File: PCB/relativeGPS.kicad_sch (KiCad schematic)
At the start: 0 parts

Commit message: Progress
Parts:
- added C1, C2: C_120pF_50V_5%_C0G_0402_H0.55, 002-Capacitors:C_0402_H0.55, symbol 002-Capacitors:C_120pF_50V_5%_C0G_0402
- added C3: C_22uF_6.3V_20%_X5R_0805_H1.4, 002-Capacitors:C_0805_H1.4, symbol 002-Capacitors:C_22uF_6.3V_20%_X5R_0805
- added C4: C_4.7uF_10V_10%_X7S_0603_H0.95, 002-Capacitors:C_0603_H0.95, symbol 002-Capacitors:C_4.7uF_10V_10%_X7S_0603
- added C5: C_10nF_50V_10%_X7R_0402_H0.55, 002-Capacitors:C_0402_H0.55, symbol 002-Capacitors:C_10nF_50V_10%_X7R_0402
- added C6: C_56pF_50V_2%_C0G_0201_H0.33, 002-Capacitors:C_0402_H0.55, symbol 002-Capacitors:C_56pF_50V_2%_C0G_0201
- added CN1: PPPC051LGBN-RC, 009-Connectors:PPPC051LGBN-RC, symbol 009-Connectors:PPPC051LGBN-RC
- added L1: L_5.6nH_2%_1.77A_40mOhm, 003-Inductors:LQW15AN5N6G80D, symbol 003-Inductors:L_5.6nH_2%_1.77A_40mOhm
- added L2: L_10uH_20%_1.51A_160mOhm, 003-Inductors:LTF5022T-100M1R3-D, symbol 003-Inductors:L_10uH_20%_1.51A_160mOhm
- added L3: L_27nH_5%_0.35A_460mOhm, 003-Inductors:LQG15HS27NJ02D, symbol 003-Inductors:L_27nH_5%_0.35A_460mOhm
- added R1: R_10k_5%_1/16W_0402, 001-Resistors:R_0402_H0.4, symbol 001-Resistors:R_10k_5%_1/16W_0402
- added R2: R_15k_1%_1/16W_0402, 001-Resistors:R_0402_H0.4, symbol 001-Resistors:R_15k_1%_1/16W_0402
- added R3: R_68k_1%_1/16W_0402, 001-Resistors:R_0402_H0.4, symbol 001-Resistors:R_68k_1%_1/16W_0402
- added R4: R_1M_5%_1/16W_0402, 001-Resistors:R_0402_H0.4, symbol 001-Resistors:R_1M_5%_1/16W_0402
- added U1: TCA39306DCUR, 005-ICs:TCA39306DCUR, symbol 005-ICs:TCA39306DCUR
- added U2: LSM303AH, 008-Sensors:LSM303AHTR, symbol 008-Sensors:LSM303AHTR
- added U3: TESEO-LIV3R, 010-RF:TESEO-LIV3R, symbol 010-RF:TESEO-LIV3R
- added U4: BGA725L6E6327FTSA1, 010-RF:BGA725L6E6327FTSA1, symbol 010-RF:BGA725L6E6327FTSA1
- added U5: B39162B4327P810, 010-RF:B39162B4327P810, symbol 010-RF:B39162B4327P810
- added U6: ST1S12GR, 004-Power:ST1S12GR, symbol 004-Power:ST1S12GR
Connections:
- new net: C2.2, U3.11 (RF_IN)
- new net: L2.1, R3.1, U6.3 (SW)
- new net: R2.1, R3.2, U6.5 (FB)
- new net: U4.3 (OUT), U5.1 (IN)
- new net: L1.2, U4.5 (IN)
- new net: R4.2, U6.1 (EN)
- new net: C4.2, R4.1, U6.4 (IN)
- new net: C2.1, U5.4 (OUT)
- new net: C1.2, L1.1
- new net +1V8: U1.2 (VREF1), U2.10 (VDD_IO), U2.2 (CS), U2.9 (VDD)
- new net +3.3V: CN1.1
- new net 3V3_TESEO: C3.1, C5.1, L2.2, L3.1
- new net 3V3_TESEO_FILTERED: C6.1, L3.2, U3.6 (Vbat), U3.7 (VCC_IO), U3.8 (VCC)
- new net ANTOFF: R1.1, U3.13 (AntOFF), U4.6 (PON)
- new net GND: C3.2, C4.1, C5.2, C6.2, CN1.5, R1.2, R2.2, U1.1 (GND), U2.6 (GND), U2.8 (GND), U4.1 (GND), U4.4 (GNDRF), U5.2 (GND), U5.3 (GND), U5.5 (GND), U6.2 (GND)
- new net RYLR998_RST: CN1.2
- new net RYLR998_RX: CN1.3
- new net RYLR998_TX: CN1.4
- new net SCL_1V8: U1.3 (SCL1), U2.1 (SCL/SPC)
- new net SDA_1V8: U1.4 (SDA1), U2.4 (SDA/SDI/SDO)
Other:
- note added: "100nF + 10uF on vdd 100nF to vdd_io"
- note added: "220nF"
- note added: "5V ?"
- note added: "GPS"
- note added: "LoRa module"
- note added: "Magnetometer + accelerometer"

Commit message: Remove useless backup files
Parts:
- added ANT1: ANT2525B00DT1516S, 010-RF:ANT2525B00DT1516S, symbol 010-RF:ANT2525B00DT1516S
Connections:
- net at C1.1: now also ANT1.1
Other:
- note added: "Add R0"
- note added: "Add jumper"
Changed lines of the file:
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@@
 	(wire
 		(pts
+			(xy 148.59 81.28) (xy 154.94 81.28)
+		)
+		(stroke
+			(width 0)
+			(type default)
+		)
+	)
+	(wire
+		(pts
 			(xy 81.28 80.01) (xy 68.58 80.01)
 		)
@@
 	(wire
 		(pts
+			(xy 148.59 78.74) (xy 148.59 81.28)
+		)
+		(stroke
+			(width 0)
+			(type default)
+		)
+	)
+	(wire
+		(pts
 			(xy 251.46 48.26) (xy 266.7 48.26)
 		)
@@
 	(wire
 		(pts
-			(xy 149.86 81.28) (xy 154.94 81.28)
-		)
-		(stroke
-			(width 0)
-			(type default)
-		)
-	)
-	(wire
-		(pts
 			(xy 254 62.23) (xy 254 68.58)
 		)
@@
 		)
 	)
+	(text "Add jumper"
+		(exclude_from_sim no)
+		(at 189.484 67.056 0)
+		(effects
+			(font
+				(size 1.27 1.27)
+			)
+		)
+	)
 	(text "220nF"
 		(exclude_from_sim no)
@@
 		)
 	)
+	(text "Add R0\n"
+		(exclude_from_sim no)
+		(at 201.93 70.104 0)
+		(effects
+			(font
+				(size 1.27 1.27)
+			)
+		)
+	)
 	(text "100nF + 10uF on vdd\n100nF to vdd_io\n"
 		(exclude_from_sim no)
@@
 					(unit 1)
 				)
+			)
+		)
+	)
+	(symbol
+		(lib_id "010-RF:ANT2525B00DT1516S")
+		(at 148.59 76.2 0)
+		(unit 1)
+		(exclude_from_sim no)
+		(in_bom yes)
+		(on_board yes)
+		(dnp no)
+		(property "Reference" "ANT1"
+			(at 139.7 74.168 0)
+			(effects
+				(font
+					(size 1.27 1.27)
+				)
+				(justify left)
+			)
+		)
+		(property "Value" "ANT2525B00DT1516S"
+			(at 148.59 86.868 0)
+			(effects
+				(font
+					(size 1.27 1.27)
+				)
+				(hide yes)
+			)
+		)
+		(property "Footprint" "010-RF:ANT2525B00DT1516S"
+			(at 148.59 99.314 0)
+			(effects
+				(font
+					(size 1.27 1.27)
+				)
+				(hide yes)
+			)
+		)
+		(property "Datasheet" "https://productfinder.pulseelectronics.com/api/open/part-attachments/datasheet/ANT2525B00DT1516S"
+			(at 148.59 93.726 0)
+			(effects
+				(font
+					(size 1.27 1.27)
+				)
+				(hide yes)
+			)
+		)
+		(property "Description" "GNSS Antenna, patch, through-hole"
+			(at 148.59 101.346 0)
+			(effects
+				(font
+					(size 1.27 1.27)
+				)
+				(hide yes)
+			)
+		)
+		(property "Web link" "https://www.digikey.ch/en/products/detail/pulse-electronics/ANT2525B00DT1516S/3927219?s=N4IgTCBcDaIIIDkAqYCsaBCAGLARJAjKgQGwDKIAugL5A"
+			(at 148.59 91.44 0)
+			(effects
+				(font
+					(size 1.27 1.27)
+				)
+				(hide yes)
+			)
+		)
+		(property "Manufacturer" "Pulse Electronics"
+			(at 148.59 88.9 0)
+			(effects
+				(font
+					(size 1.27 1.27)
+				)
+				(hide yes)
+			)
+		)
+		(property "Manufacturer P/N" "ANT2525B00DT1516S"
+			(at 148.844 103.632 0)
+			(effects
+				(font
+					(size 1.27 1.27)
+				)
+				(hide yes)
+			)
+		)
+		(property "Digikey P/N" "311-1539-ND"
+			(at 148.844 96.266 0)
+			(effects
+				(font
+					(size 1.27 1.27)
+				)
+				(hide yes)
+			)
+		)
+		(property "Price" "2.48"
+			(at 148.59 108.204 0)
+			(effects
+				(font
+					(size 1.27 1.27)
+				)
+				(hide yes)
+			)
+		)
+		(property "Height" "4"
+			(at 148.59 109.982 0)
+			(effects
+				(font
+					(size 1.27 1.27)
+				)
+				(hide yes)
+			)
+		)
+		(property "Temperature" "-40 to 105"
+			(at 148.59 105.918 0)
+			(effects
+				(font
+					(size 1.27 1.27)
+				)
+				(hide yes)
+			)
+		)
+		(property "Value Disp" "ANT 25x25"
+			(at 136.144 76.454 0)
+			(effects
+				(font
+					(size 1.27 1.27)
+				)
+				(justify left)
+			)
+		)
+		(pin "1"
+		)
+		(instances
+			(project "relativeGPS"
+				(path "/9255e348-2f0c-48d3-8a71-46491dcb1a12"
+					(reference "ANT1")
+					(unit 1)
+				)

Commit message: WIP
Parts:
- removed ANT1: ANT2525B00DT1516S, 010-RF:ANT2525B00DT1516S, symbol 010-RF:ANT2525B00DT1516S
- removed C1, C2: C_120pF_50V_5%_C0G_0402_H0.55, 002-Capacitors:C_0402_H0.55, symbol 002-Capacitors:C_120pF_50V_5%_C0G_0402
- removed C3: C_22uF_6.3V_20%_X5R_0805_H1.4, 002-Capacitors:C_0805_H1.4, symbol 002-Capacitors:C_22uF_6.3V_20%_X5R_0805
- removed C4: C_4.7uF_10V_10%_X7S_0603_H0.95, 002-Capacitors:C_0603_H0.95, symbol 002-Capacitors:C_4.7uF_10V_10%_X7S_0603
- removed C5: C_10nF_50V_10%_X7R_0402_H0.55, 002-Capacitors:C_0402_H0.55, symbol 002-Capacitors:C_10nF_50V_10%_X7R_0402
- removed C6: C_56pF_50V_2%_C0G_0201_H0.33, 002-Capacitors:C_0402_H0.55, symbol 002-Capacitors:C_56pF_50V_2%_C0G_0201
- removed L1: L_5.6nH_2%_1.77A_40mOhm, 003-Inductors:LQW15AN5N6G80D, symbol 003-Inductors:L_5.6nH_2%_1.77A_40mOhm
- removed L2: L_10uH_20%_1.51A_160mOhm, 003-Inductors:LTF5022T-100M1R3-D, symbol 003-Inductors:L_10uH_20%_1.51A_160mOhm
- removed L3: L_27nH_5%_0.35A_460mOhm, 003-Inductors:LQG15HS27NJ02D, symbol 003-Inductors:L_27nH_5%_0.35A_460mOhm
- removed R1: R_10k_5%_1/16W_0402, 001-Resistors:R_0402_H0.4, symbol 001-Resistors:R_10k_5%_1/16W_0402
- removed R2: R_15k_1%_1/16W_0402, 001-Resistors:R_0402_H0.4, symbol 001-Resistors:R_15k_1%_1/16W_0402
- removed R3: R_68k_1%_1/16W_0402, 001-Resistors:R_0402_H0.4, symbol 001-Resistors:R_68k_1%_1/16W_0402
- removed R4: R_1M_5%_1/16W_0402, 001-Resistors:R_0402_H0.4, symbol 001-Resistors:R_1M_5%_1/16W_0402
- removed U1: TCA39306DCUR, 005-ICs:TCA39306DCUR, symbol 005-ICs:TCA39306DCUR
- removed U2: LSM303AH, 008-Sensors:LSM303AHTR, symbol 008-Sensors:LSM303AHTR
- removed U3: TESEO-LIV3R, 010-RF:TESEO-LIV3R, symbol 010-RF:TESEO-LIV3R
- removed U4: BGA725L6E6327FTSA1, 010-RF:BGA725L6E6327FTSA1, symbol 010-RF:BGA725L6E6327FTSA1
- removed U5: B39162B4327P810, 010-RF:B39162B4327P810, symbol 010-RF:B39162B4327P810
- removed U6: ST1S12GR, 004-Power:ST1S12GR, symbol 004-Power:ST1S12GR
- added C10, C11, C9: C_1uF_50V_10%_X5R_0603_H0.9, 002-Capacitors:C_0603_H0.95, symbol 002-Capacitors:C_1uF_50V_10%_X5R_0603
- added C8: C_100nF_50V_10%_X7R_0402_H0.55, 002-Capacitors:C_0402_H0.55, symbol 002-Capacitors:C_100nF_50V_10%_X7R_0402
- added IC1: MIC5330-SSYML-TR, 004-Power:MIC5330, symbol 004-Power:MIC5330-SSYML-TR
- added R10, R9: R_4k7_1%_1/10W_0603, 001-Resistors:R_0603_H0.55, symbol 001-Resistors:R_4k7_1%_1/10W_0603
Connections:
- net +3.3V: now also C10.1, IC1.8 (VOUT1), R10.1, R9.1; no longer CN1.1
- net GND: now also C10.2, C11.2, C8.2, C9.2, IC1.2 (GND)
- new net: C8.1, IC1.3 (BYP)
- new net +3.3V_RYLR: C11.1, CN1.1, IC1.7 (VOUT2)
- new net +5V: C9.1, IC1.1 (VIN), IC1.5 (EN1)
- new net RYLR_3V3_EN: IC1.4 (EN2)
- new net SCL: R9.2
- new net SDA: R10.2
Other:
- added sheet GPS (GPS.kicad_sch)
- added sheet MAG_ACC (MAG_ACC.kicad_sch)
- note added: "1V8 generation"
- note added: "Battery + 5V generation"
- note added: "LEDs"
- note added: "MCU"
- note removed: "100nF + 10uF on vdd 100nF to vdd_io"
- note removed: "220nF"
- note removed: "5V ?"
- note removed: "Add R0"
- note removed: "Add jumper"
- note removed: "GPS"
- note removed: "Magnetometer + accelerometer"

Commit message: WIP
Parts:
- removed C10, C11, C9: C_1uF_50V_10%_X5R_0603_H0.9, 002-Capacitors:C_0603_H0.95, symbol 002-Capacitors:C_1uF_50V_10%_X5R_0603
- removed C8: C_100nF_50V_10%_X7R_0402_H0.55, 002-Capacitors:C_0402_H0.55, symbol 002-Capacitors:C_100nF_50V_10%_X7R_0402
- removed CN1: PPPC051LGBN-RC, 009-Connectors:PPPC051LGBN-RC, symbol 009-Connectors:PPPC051LGBN-RC
- removed IC1: MIC5330-SSYML-TR, 004-Power:MIC5330, symbol 004-Power:MIC5330-SSYML-TR
- added CN1: 5PTH_connector, 009-Connectors:5-PTH_connector, symbol 009-Connectors:5PTH_connector
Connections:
- net +3.3V_RYLR: now also CN1.1
- net GND: now also CN1.5
- net RYLR998_RST: now also CN1.2
- net RYLR998_RX: now also CN1.3
- net RYLR998_TX: now also CN1.4
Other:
- added sheet POWER (POWER.kicad_sch)
- note added: "Buttons / switches"
- note removed: "Battery + 5V generation"
- moved on the sheet: R10, R9

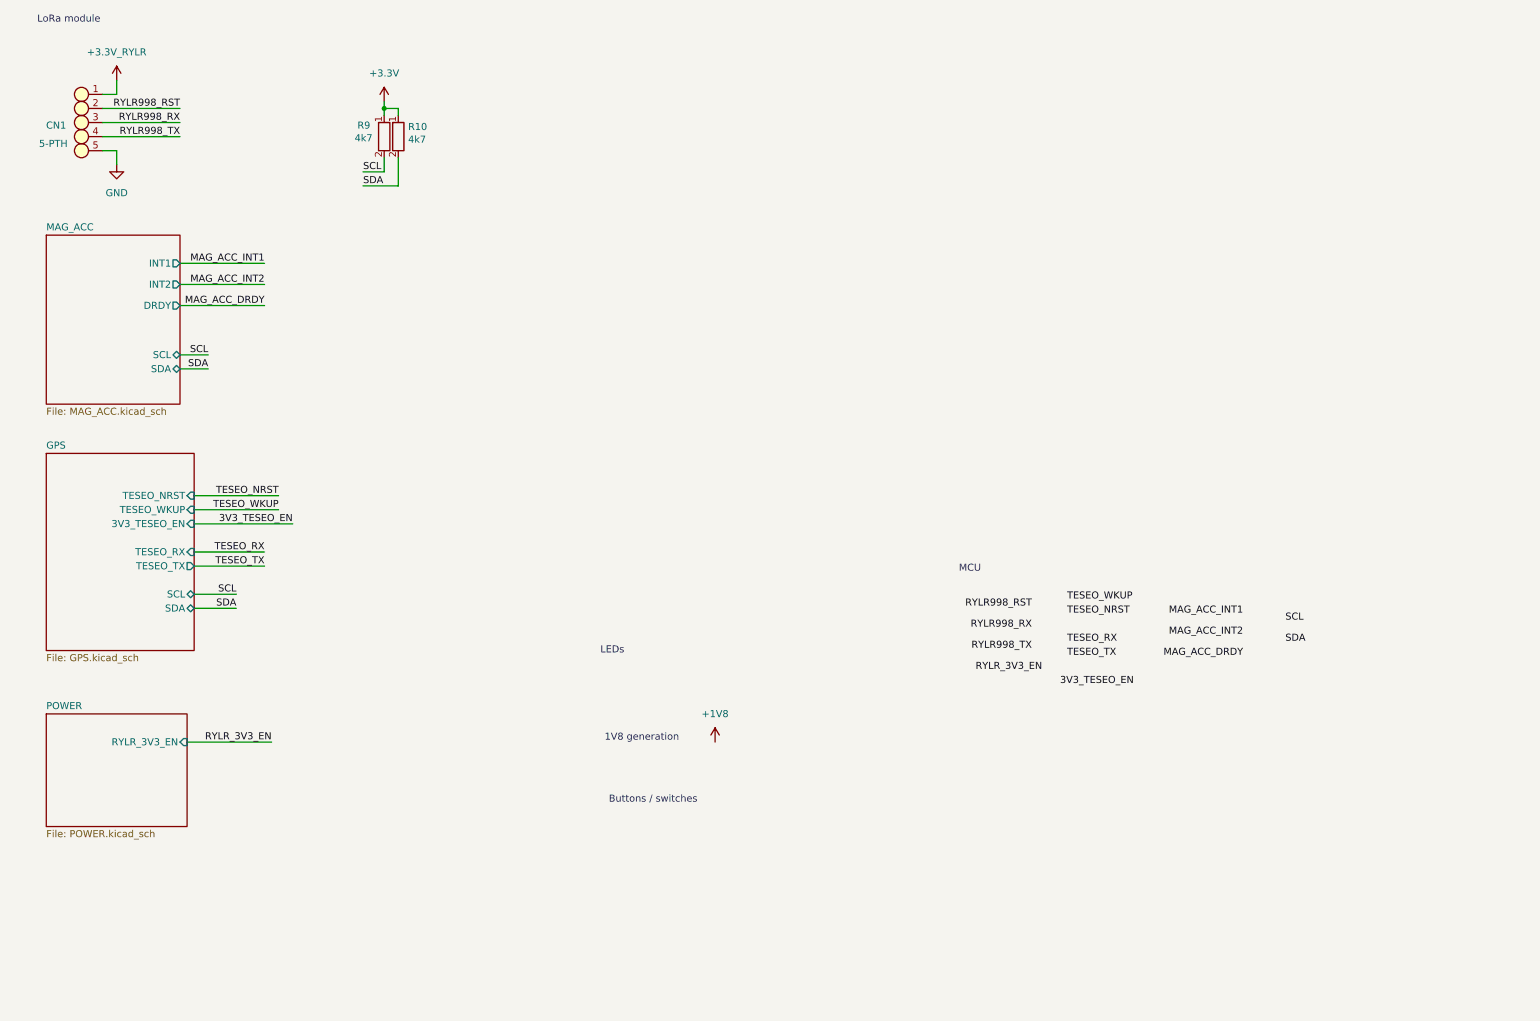
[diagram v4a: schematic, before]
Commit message: Add LEDs
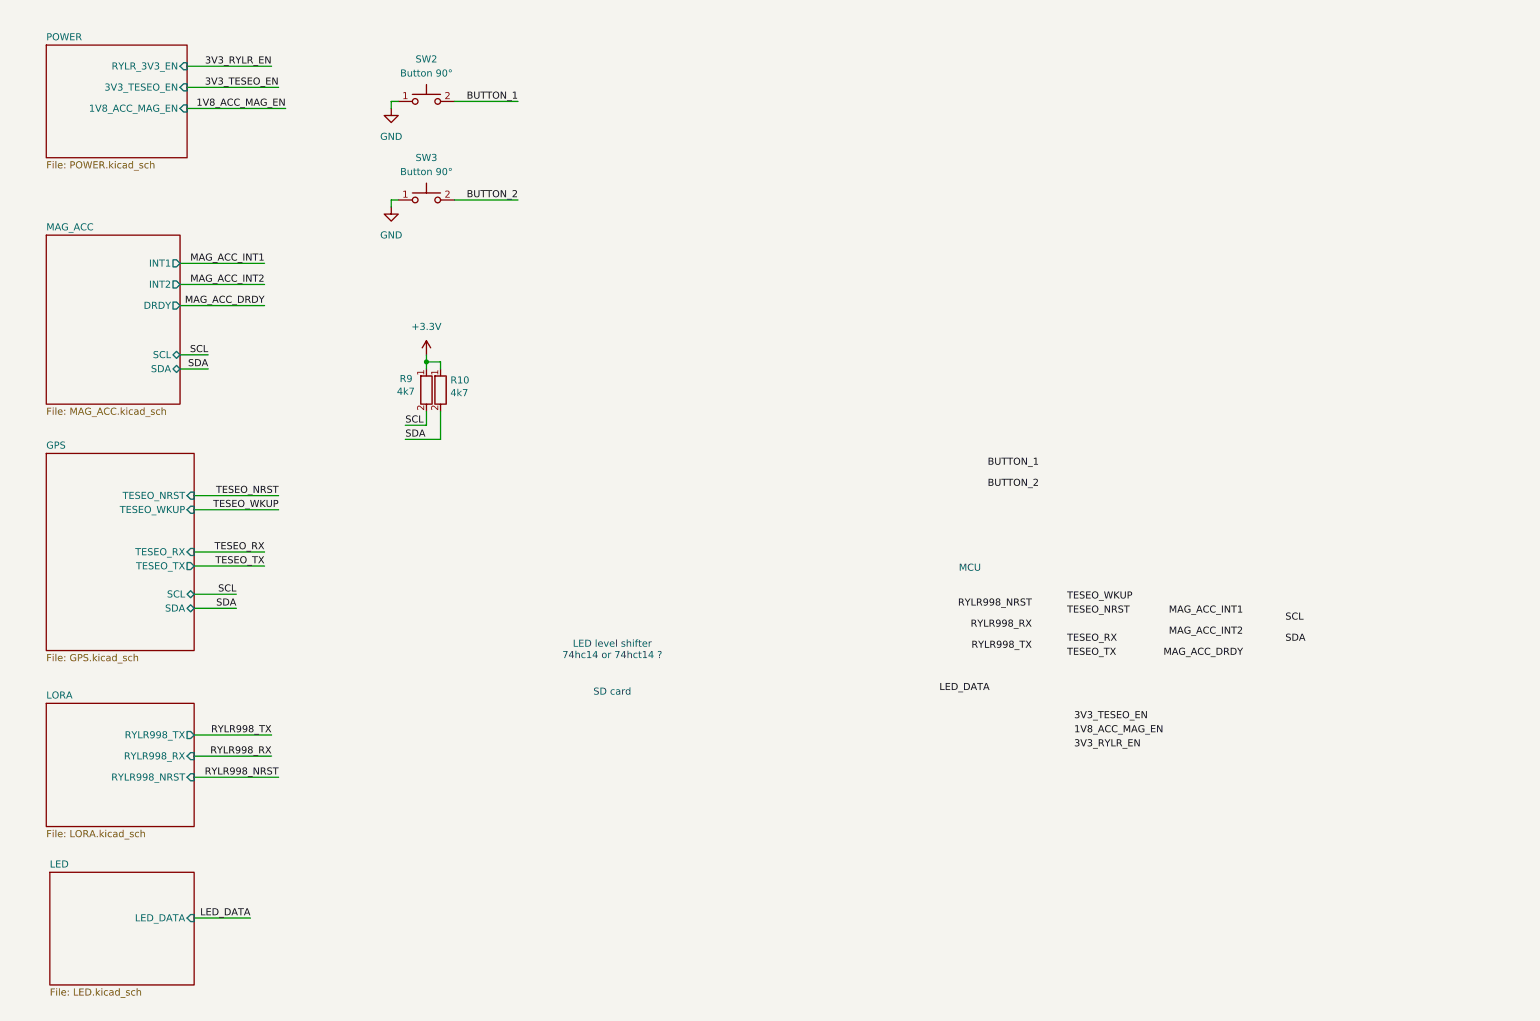
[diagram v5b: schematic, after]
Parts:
- removed CN1: 5PTH_connector, 009-Connectors:5-PTH_connector, symbol 009-Connectors:5PTH_connector
- added SW2, SW3: EVQ-P7A01P, 009-Connectors:EVQ-P7A01P, symbol 009-Connectors:EVQ-P7A01P
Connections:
- net GND: now also SW2.1, SW3.1
- new net BUTTON_1: SW2.2
- new net BUTTON_2: SW3.2
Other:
- added sheet LED (LED.kicad_sch)
- added sheet LORA (LORA.kicad_sch)
- sheet GPS ports: added none; removed 3V3_TESEO_EN
- sheet POWER ports: added 1V8_ACC_MAG_EN, 3V3_TESEO_EN; removed none
- note added: "LED level shifter 74hc14 or 74hct14 ?"
- note added: "SD card"
- note removed: "1V8 generation"
- note removed: "Buttons / switches"
- note removed: "LEDs"
- note removed: "LoRa module"
- moved on the sheet: R10, R9
